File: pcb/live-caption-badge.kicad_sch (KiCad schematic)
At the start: 26 parts, among them J1 USB_C_Receptacle_USB2.0_14P, J4 Conn_01x04_Socket, SW1 KILL, SW2 RST, U1 ESP32-S3-WROOM-1, U2 HE9073A33M5R, U4 HE9073A33M5R

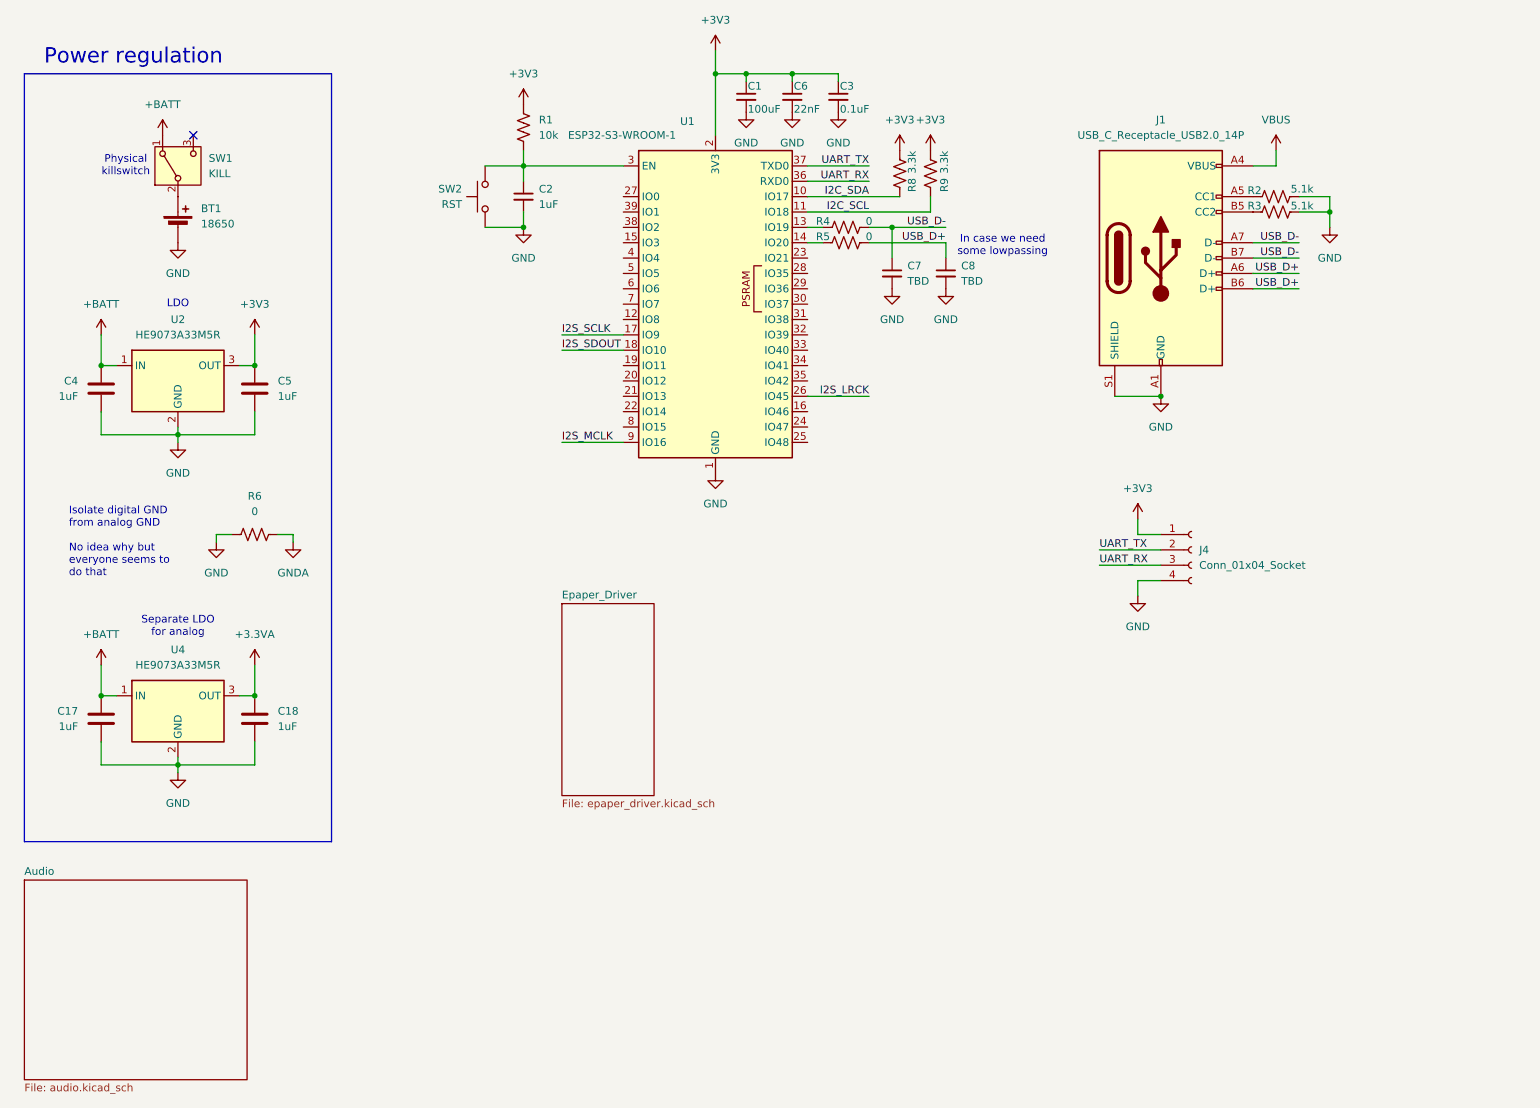
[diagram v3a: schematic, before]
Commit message: pcb: Audio subschematic seems done
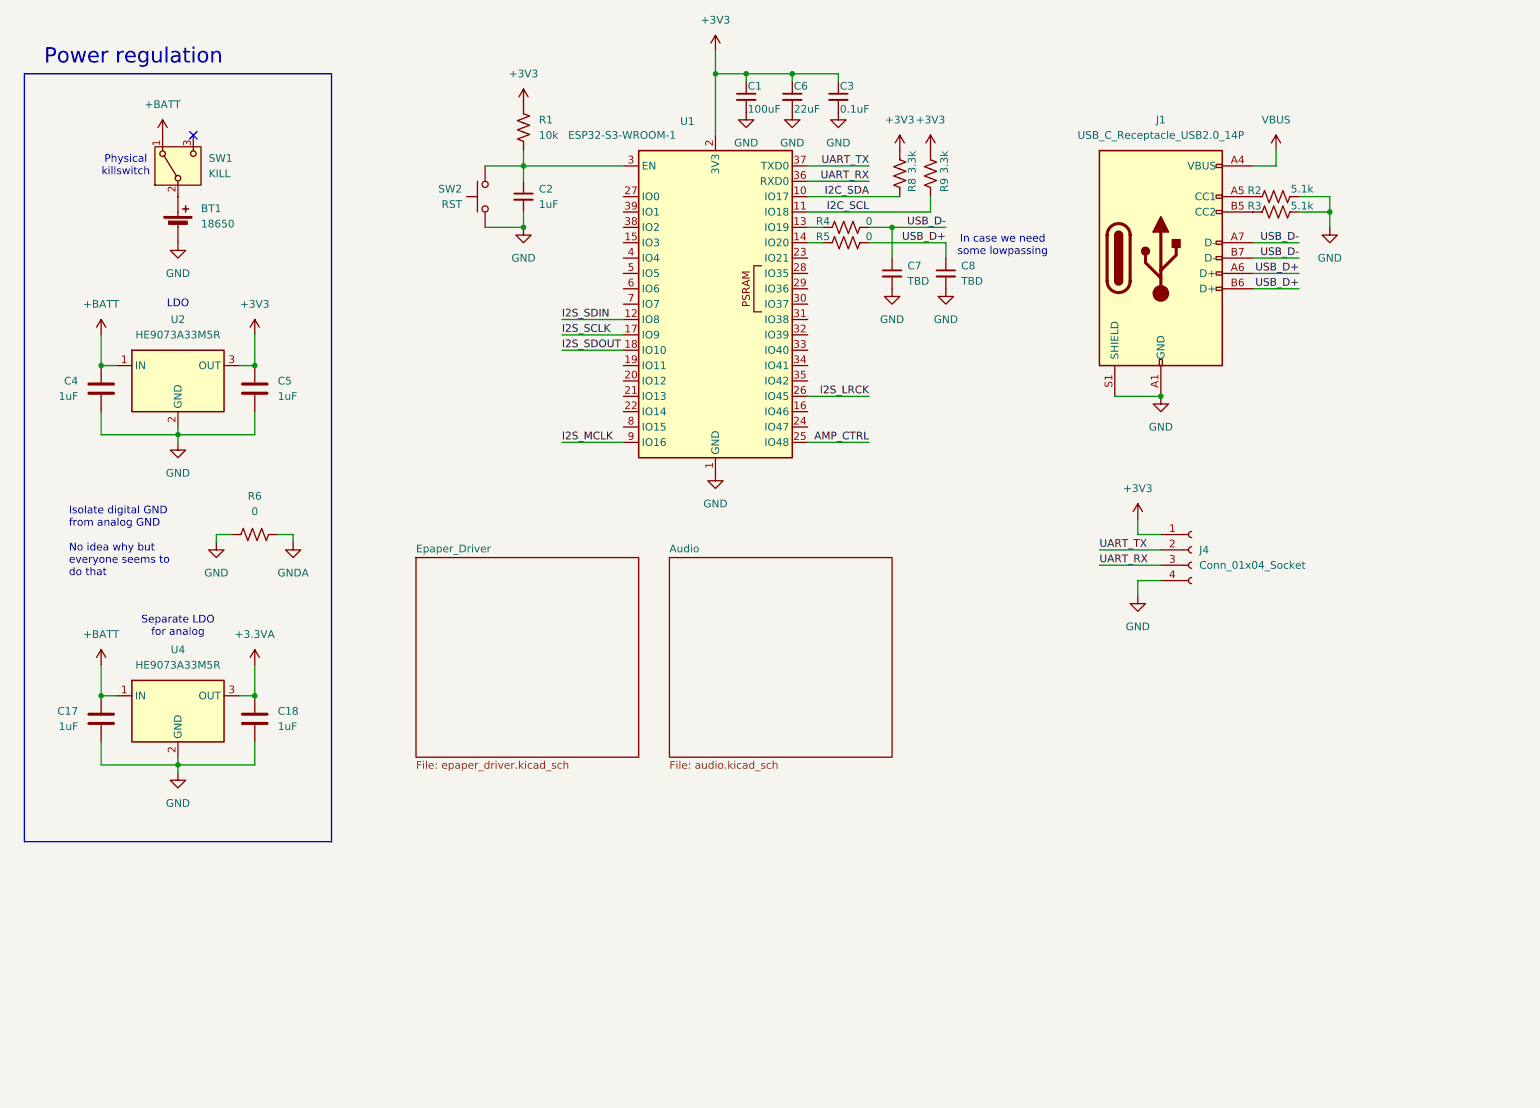
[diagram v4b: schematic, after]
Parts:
- C6: value 22nF -> 22uF
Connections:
- net I2S_SDIN: now reaches U1.12 (IO8)
- net AMP_CTRL: now reaches U1.25 (IO48)
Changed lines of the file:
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@@
 	(wire
 		(pts
+			(xy 154.94 86.36) (xy 165.1 86.36)
+		)
+		(stroke
+			(width 0)
+			(type default)
+		)
+	)
+	(wire
+		(pts
 			(xy 38.1 135.89) (xy 38.1 139.7)
 		)
@@
 	(wire
 		(pts
+			(xy 114.3 66.04) (xy 124.46 66.04)
+		)
+		(stroke
+			(width 0)
+			(type default)
+		)
+	)
+	(wire
+		(pts
 			(xy 203.2 104.14) (xy 213.36 104.14)
 		)
@@
 		)
 	)
+	(label "I2S_SDIN"
+		(at 114.3 66.04 0)
+		(fields_autoplaced yes)
+		(effects
+			(font
+				(size 1.27 1.27)
+			)
+			(justify left bottom)
+		)
+	)
 	(label "USB_D+"
 		(at 177.8 53.34 180)
@@
 		)
 	)
+	(label "AMP_CTRL"
+		(at 165.1 86.36 180)
+		(fields_autoplaced yes)
+		(effects
+			(font
+				(size 1.27 1.27)
+			)
+			(justify right bottom)
+		)
+	)
 	(label "UART_RX"
 		(at 165.1 43.18 180)
@@
 			)
 		)
-		(property "Value" "22nF"
+		(property "Value" "22uF"
 			(at 152.654 31.242 0)
 			(effects
@@
 	)
 	(sheet
-		(at 114.3 113.03)
-		(size 15.24 31.75)
+		(at 90.17 105.41)
+		(size 36.83 33.02)
 		(fields_autoplaced yes)
 		(stroke
@@
 		)
 		(property "Sheetname" "Epaper_Driver"
-			(at 114.3 112.3184 0)
+			(at 90.17 104.6984 0)
 			(effects
 				(font
@@
 		)
 		(property "Sheetfile" "epaper_driver.kicad_sch"
-			(at 114.3 145.3646 0)
+			(at 90.17 139.0146 0)
 			(effects
 				(font
@@
 	)
 	(sheet
-		(at 25.4 158.75)
+		(at 132.08 105.41)
 		(size 36.83 33.02)
 		(fields_autoplaced yes)
@@
 		)
 		(property "Sheetname" "Audio"
-			(at 25.4 158.0384 0)
+			(at 132.08 104.6984 0)
 			(effects
 				(font
@@
 		)
 		(property "Sheetfile" "audio.kicad_sch"
-			(at 25.4 192.3546 0)
+			(at 132.08 139.0146 0)
 			(effects
 				(font

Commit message: pcb: Schematics seem complete
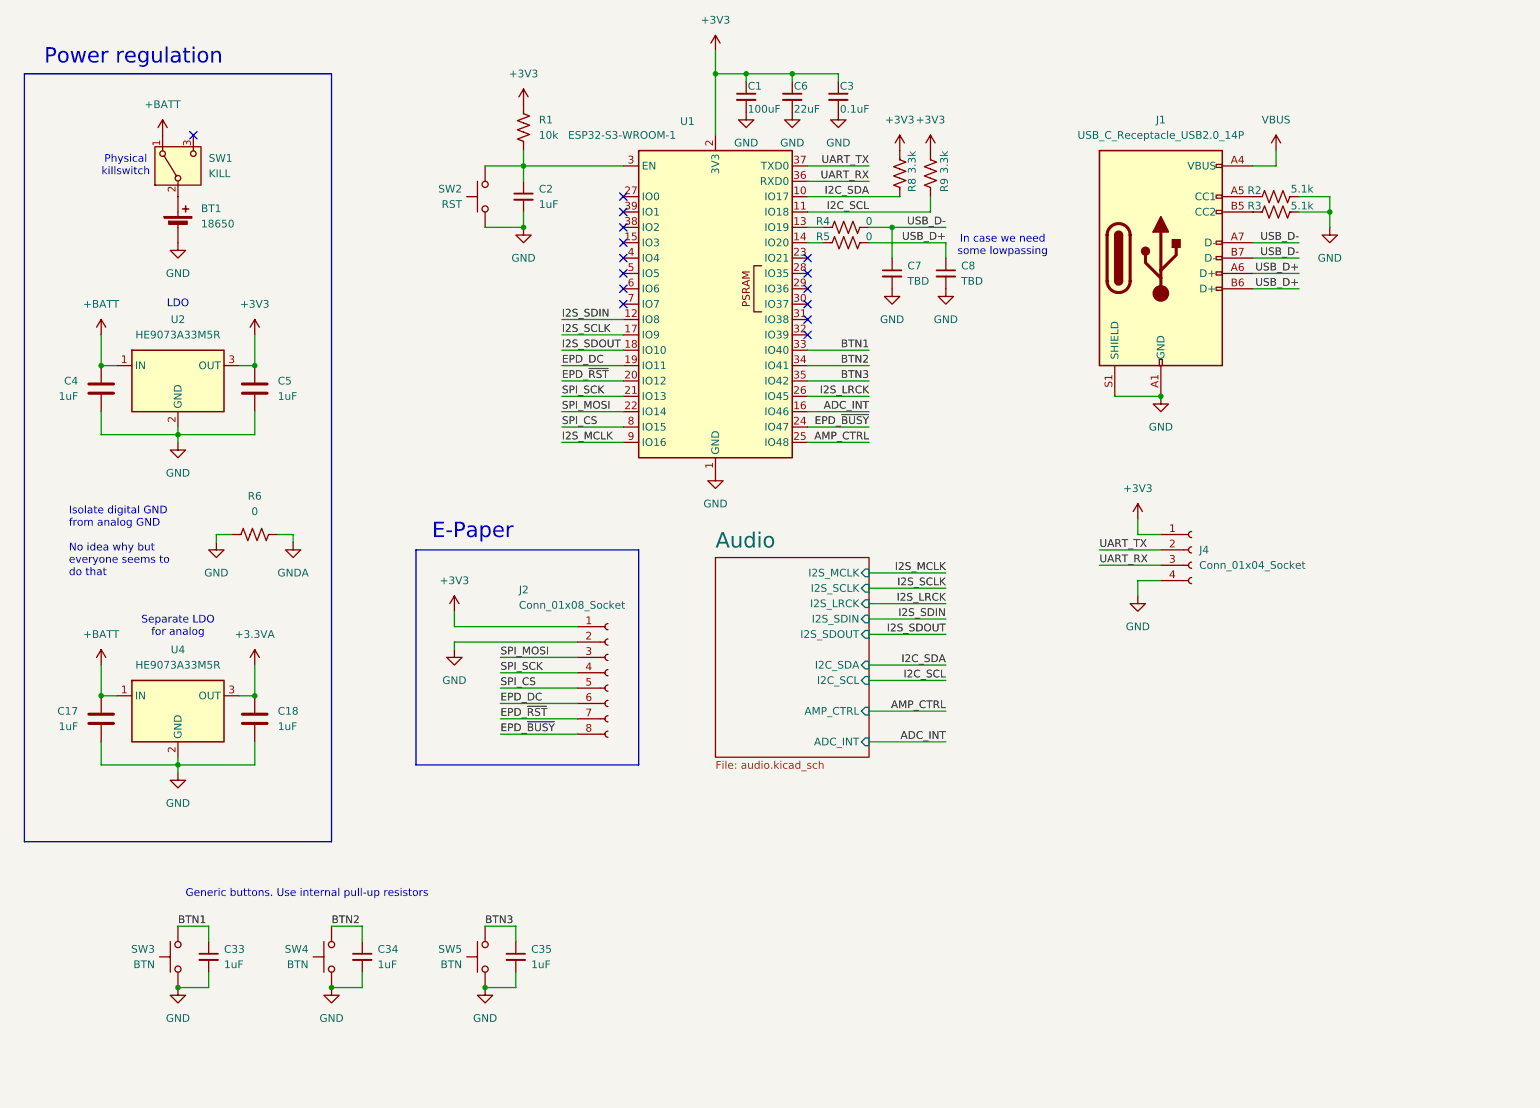
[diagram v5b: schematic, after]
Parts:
- added C33, C34, C35: 1uF, symbol Device:C_Small
- added J2: Conn_01x08_Socket, symbol Connector:Conn_01x08_Socket
- added SW3, SW4, SW5: BTN, symbol Switch:SW_Push
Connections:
- net +3V3: now also J2.1 (Pin_1)
- net GND: now also C33.2, C34.2, C35.2, J2.2 (Pin_2), SW3.1, SW4.1, SW5.1
- net ADC_INT: now reaches U1.16 (IO46)
- net EPD_DC: now reaches U1.19 (IO11)
- net EPD_DC: now also J2.6 (Pin_6)
- net EPD_~{RST}: now reaches U1.20 (IO12)
- net EPD_~{RST}: now also J2.7 (Pin_7)
- net SPI_SCK: now reaches U1.21 (IO13)
- net SPI_SCK: now also J2.4 (Pin_4)
- net SPI_MOSI: now reaches U1.22 (IO14)
- net SPI_MOSI: now also J2.3 (Pin_3)
- net EPD_~{BUSY}: now reaches U1.24 (IO47)
- net EPD_~{BUSY}: now also J2.8 (Pin_8)
- net BTN1: now reaches U1.33 (IO40)
- net BTN1: now also C33.1, SW3.2
- net BTN2: now reaches U1.34 (IO41)
- net BTN2: now also C34.1, SW4.2
- net BTN3: now reaches U1.35 (IO42)
- net BTN3: now also C35.1, SW5.2
- net SPI_CS: now reaches U1.8 (IO15)
- net SPI_CS: now also J2.5 (Pin_5)
- no-connect marks 1 -> 15
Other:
- removed sheet Epaper_Driver
- sheet Audio ports: added ADC_INT, AMP_CTRL, I2C_SCL, I2C_SDA, I2S_LRCK, I2S_MCLK, I2S_SCLK, I2S_SDIN, I2S_SDOUT; removed none
- note added: "E-Paper"
- note added: "Generic buttons. Use internal pull-up resistors"

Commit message: pcb: Renumber parts
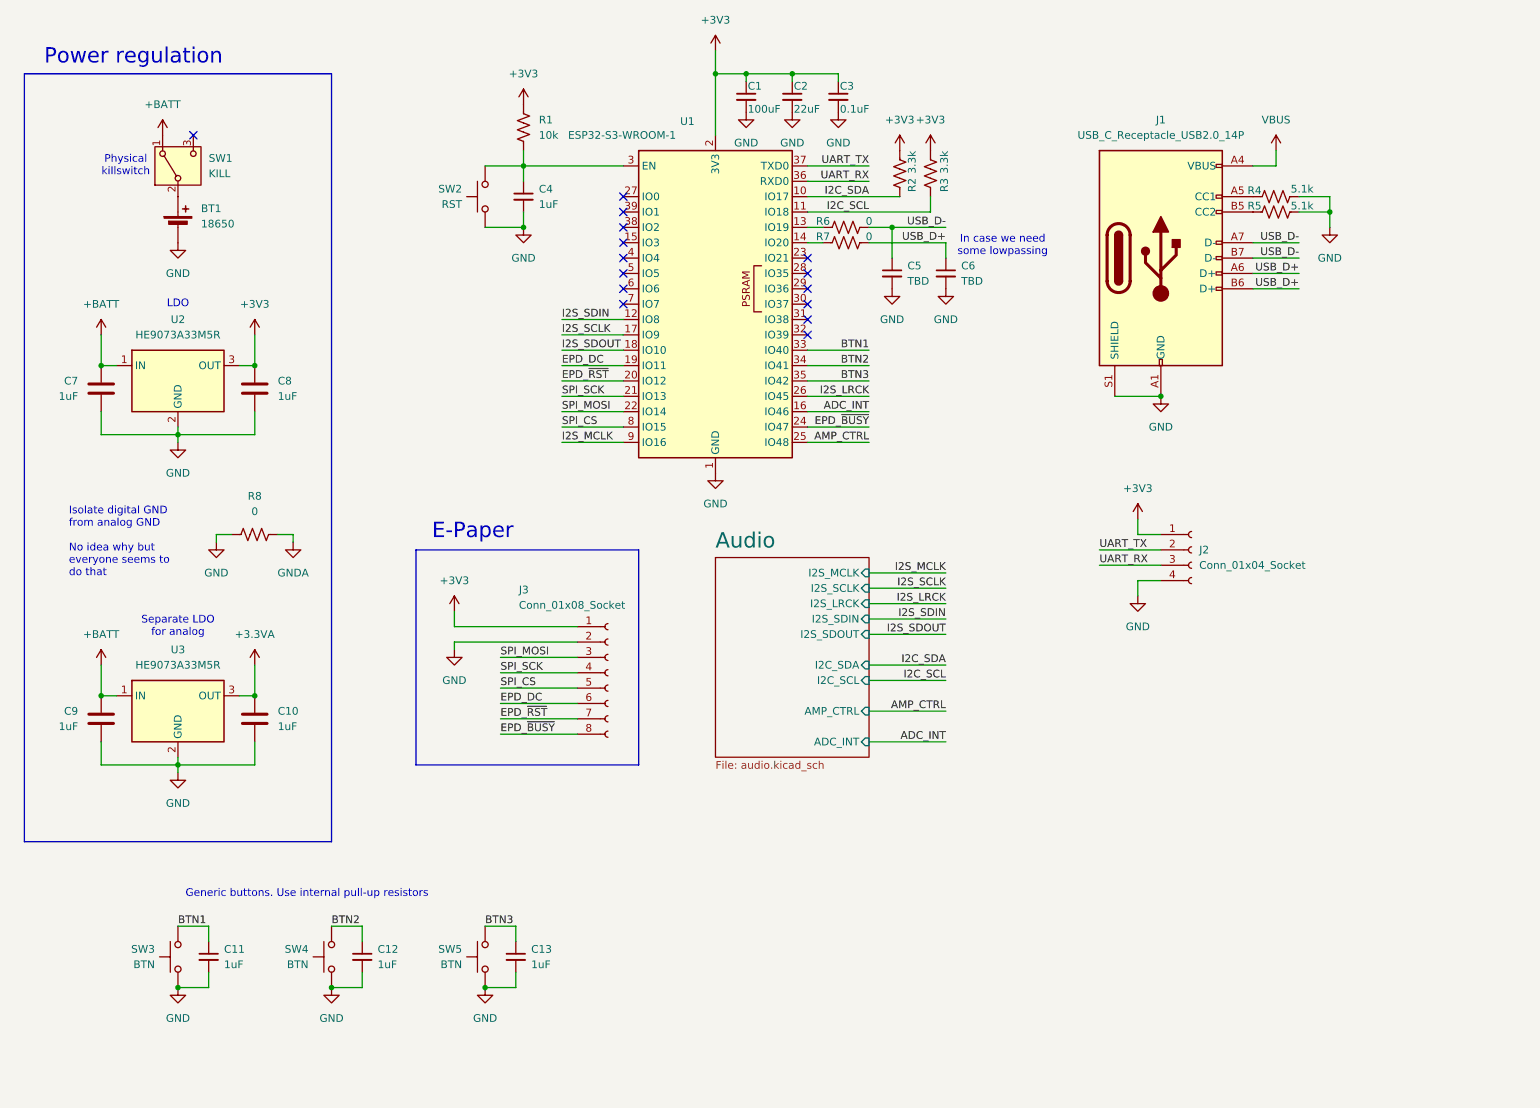
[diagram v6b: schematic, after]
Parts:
- renumbered C18 to C10, C33 to C11, C34 to C12, C35 to C13, C6 to C2, C2 to C4, C7 to C5, C8 to C6, C4 to C7, C5 to C8, C17 to C9, J4 to J2, J2 to J3, R8 to R2, R9 to R3, R2 to R4, R3 to R5, R4 to R6, R5 to R7, R6 to R8, U4 to U3

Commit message: pcb: Assigned footprints (the more trivial ones)
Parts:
- C1, C10, C11, C12, C13, C2, C3, C4, C5, C6, C7, C8, C9: footprint (none) -> Capacitor_SMD:C_0603_1608Metric
- J2: footprint (none) -> Connector_PinSocket_2.54mm:PinSocket_1x04_P2.54mm_Vertical
- J3: footprint (none) -> Connector_PinSocket_2.00mm:PinSocket_1x08_P2.00mm_Horizontal
- R1, R2, R3, R4, R5, R6, R7, R8: footprint (none) -> Resistor_SMD:R_0603_1608Metric
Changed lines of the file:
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@@
 	(generator "eeschema")
 	(generator_version "8.0")
-	(paper "USLetter")
+	(paper "A4")
 	(title_block
 		(title "Live Caption Badge")
-		(date "2024-10-17")
+		(date "2024-10-27")
 		(company "EECS 473 Fall 2024 Team 9")
 	)
@@
 			)
 		)
-		(property "Footprint" ""
+		(property "Footprint" "Resistor_SMD:R_0603_1608Metric"
 			(at 232.664 47.244 90)
 			(effects
@@
 			)
 		)
-		(property "Footprint" ""
+		(property "Footprint" "Capacitor_SMD:C_0603_1608Metric"
 			(at 107.95 45.72 0)
 			(effects
@@
 			)
 		)
-		(property "Footprint" ""
+		(property "Footprint" "Capacitor_SMD:C_0603_1608Metric"
 			(at 81.28 171.45 0)
 			(effects
@@
 			)
 		)
-		(property "Footprint" ""
+		(property "Footprint" "Capacitor_SMD:C_0603_1608Metric"
 			(at 64.4652 81.28 0)
 			(effects
@@
 			)
 		)
-		(property "Footprint" ""
+		(property "Footprint" "Resistor_SMD:R_0603_1608Metric"
 			(at 232.664 44.704 90)
 			(effects
@@
 			)
 		)
-		(property "Footprint" ""
+		(property "Footprint" "Resistor_SMD:R_0603_1608Metric"
 			(at 176.276 42.164 90)
 			(effects
@@
 			)
 		)
-		(property "Footprint" ""
+		(property "Footprint" "Capacitor_SMD:C_0603_1608Metric"
 			(at 37.1348 135.89 0)
 			(effects
@@
 			)
 		)
-		(property "Footprint" ""
+		(property "Footprint" "Capacitor_SMD:C_0603_1608Metric"
 			(at 177.8 58.42 0)
 			(effects
@@
 			)
 		)
-		(property "Footprint" ""
+		(property "Footprint" "Capacitor_SMD:C_0603_1608Metric"
 			(at 37.1348 81.28 0)
 			(effects
@@
 			)
 		)
-		(property "Footprint" ""
+		(property "Footprint" "Resistor_SMD:R_0603_1608Metric"
 			(at 108.966 34.544 90)
 			(effects
@@
 			)
 		)
-		(property "Footprint" ""
+		(property "Footprint" "Connector_PinSocket_2.54mm:PinSocket_1x04_P2.54mm_Vertical"
 			(at 218.44 104.14 0)
 			(effects
@@
 			)
 		)
-		(property "Footprint" ""
+		(property "Footprint" "Capacitor_SMD:C_0603_1608Metric"
 			(at 55.88 171.45 0)
 			(effects
@@
 			)
 		)
-		(property "Footprint" ""
+		(property "Footprint" "Capacitor_SMD:C_0603_1608Metric"
 			(at 144.78 29.21 0)
 			(effects
@@
 			)
 		)
-		(property "Footprint" ""
+		(property "Footprint" "Connector_PinSocket_2.00mm:PinSocket_1x08_P2.00mm_Horizontal"
 			(at 121.92 124.46 0)
 			(effects
@@
 			)
 		)
-		(property "Footprint" ""
+		(property "Footprint" "Capacitor_SMD:C_0603_1608Metric"
 			(at 168.91 58.42 0)
 			(effects
@@
 			)
 		)
-		(property "Footprint" ""
+		(property "Footprint" "Resistor_SMD:R_0603_1608Metric"
 			(at 63.754 100.584 90)
 			(effects
@@
 			)
 		)
-		(property "Footprint" ""
+		(property "Footprint" "Capacitor_SMD:C_0603_1608Metric"
 			(at 106.68 171.45 0)
 			(effects
@@
 			)
 		)
-		(property "Footprint" ""
+		(property "Footprint" "Capacitor_SMD:C_0603_1608Metric"
 			(at 160.02 29.21 0)
 			(effects
@@
 			)
 		)
-		(property "Footprint" ""
+		(property "Footprint" "Capacitor_SMD:C_0603_1608Metric"
 			(at 64.4652 135.89 0)
 			(effects
@@
 			)
 		)
-		(property "Footprint" ""
+		(property "Footprint" "Resistor_SMD:R_0603_1608Metric"
 			(at 171.196 42.164 90)
 			(effects
@@
 			)
 		)
-		(property "Footprint" ""
+		(property "Footprint" "Capacitor_SMD:C_0603_1608Metric"
 			(at 152.4 29.21 0)
 			(effects
@@
 			)
 		)
-		(property "Footprint" ""
+		(property "Footprint" "Resistor_SMD:R_0603_1608Metric"
 			(at 161.544 49.784 90)
 			(effects
@@
 			)
 		)
-		(property "Footprint" ""
+		(property "Footprint" "Resistor_SMD:R_0603_1608Metric"
 			(at 161.544 52.324 90)
 			(effects

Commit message: pcb: Begin layout
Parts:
- removed U3: HE9073A33M5R, symbol Regulator_Linear:LT1963AxST-3.3
- added U3: HE9073A33M5R, Package_TO_SOT_SMD:SOT-23-5, symbol live-caption-badge:HE9073A33M5R
- C10, C7, C8, C9: value 1uF -> 10uF
- U2: footprint (none) -> Package_TO_SOT_SMD:SOT-23-5; symbol Regulator_Linear:LT1963AxST-3.3 -> live-caption-badge:HE9073A33M5R
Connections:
- net +3.3VA: now also U3.5 (OUT)
- net +3V3: now also U2.5 (OUT); no longer U2.3 (OUT)
- net +BATT: now also U2.3 (CE), U3.1 (IN), U3.3 (CE)
- net GND: now also U3.2 (GND)
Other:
- moved on the sheet: C10, C7, C8, C9
